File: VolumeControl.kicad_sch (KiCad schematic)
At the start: 8 parts, among them U6 NE5532, U7 NE5532

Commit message: Complete Volume Control
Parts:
- added C13, C19: 220u, symbol Device:C_Polarized
- added C14, C21: C, symbol Device:C
- added C15, C16, C22, C23: 100p, symbol Device:C
- added C17, C24: 470p, symbol Device:C
- added C18, C20: 100n, symbol Device:C
- added J1, J2: Conn_01x03, symbol Connector_Generic:Conn_01x03
- added R25, R31, R34, R35, R36, R37, R43: 1k, symbol Device:R
- added R26, R28, R38, R39: 5k6, symbol Device:R
- added R27, R29, R40, R41: 10, symbol Device:R
- added R30, R32, R42, R44: 3k3, symbol Device:R
- added R33: 47k, symbol Device:R
- added U8, U9: NE5532, symbol Amplifier_Operational:NE5532
- R21: value 10 -> 47k
- R22, R23, R24: value 10 -> 1k
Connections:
- net +15V: now also C18.1, C20.1, U8.8 (V+), U9.8 (V+)
- net GND: now also C18.2, C20.2, U8.4 (V-), U9.4 (V-)
- net INP_BUF_OUT_RIGHT: now also C19.1; no longer R21.2, R22.2, R23.2, R24.2
- net at U6.5 (+): now also R21.2, C14.2; no longer U6.3 (+)
- net at R22.1, U6.6 (-), U6.7: now also R25.1
- net at U7.5 (+): now also R31.1; no longer U7.3 (+)
- new net: C16.2, R28.1, R29.2, U7.1
- new net: C16.1, R25.2, R28.2, U7.2 (-)
- new net: C13.2, J1.1 (Pin_1)
- new net: J1.3 (Pin_3), R27.1, R29.1, R32.2
- new net: C22.1, R36.2, R38.2, U9.2 (-)
- new net: C22.2, R38.1, R40.2, U9.1
- new net: C17.1, R30.2, R32.1, U7.6 (-)
- new net: C15.1, R22.2, R26.2, U6.2 (-)
- new net: C15.2, R26.1, R27.2, U6.1
- new net: R23.1, U7.3 (+)
- new net: R34.1, U9.3 (+)
- new net: C23.2, R39.1, R41.2, U8.1
- new net: C23.1, R37.2, R39.2, U8.2 (-)
- new net: R35.1, U8.3 (+)
- new net: R36.1, R37.1, U9.6 (-), U9.7
- new net: C24.1, R42.1, R44.2, U8.6 (-)
- new net: J2.3 (Pin_3), R40.1, R41.1, R42.2
- new net: C21.2, R33.2, U9.5 (+)
- new net: R43.1, U8.5 (+)
- new net: R24.1, U6.3 (+)
- new net: C19.2, J2.1 (Pin_1)
- new net INP_BUF_OUT_LEFT: C13.1
- new net VAS_OUT_LEFT: C17.2, R30.1, U7.7
- new net VAS_OUT_RIGHT: C24.2, R44.1, U8.7
- new net VBIAS_LEFT: R21.1, R23.2, R24.2, R31.2
- new net VBIAS_RIGHT: R33.1, R34.2, R35.2, R43.2
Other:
- note added: "Baxandall Active Volume Control"
- moved on the sheet: C11, C12, R21, R22, U6A, U6B, U6C, U7B, U7C

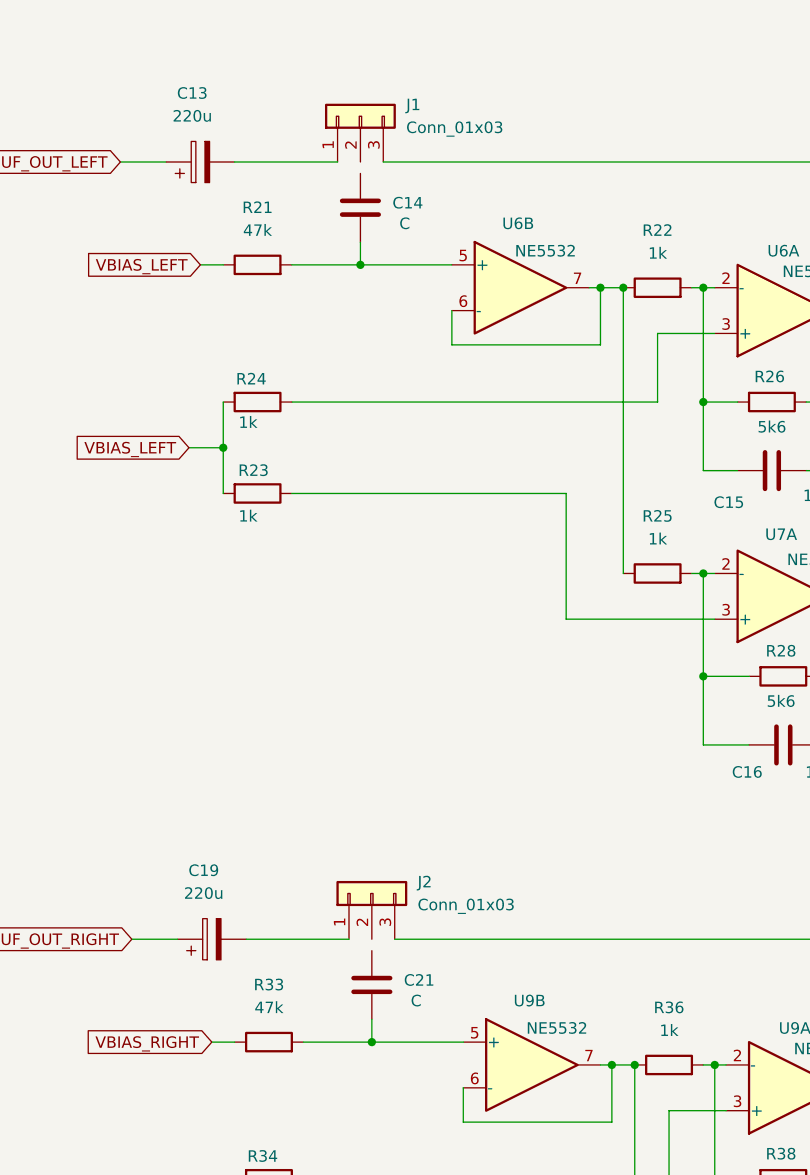
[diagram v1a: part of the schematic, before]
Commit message: Add missing C values
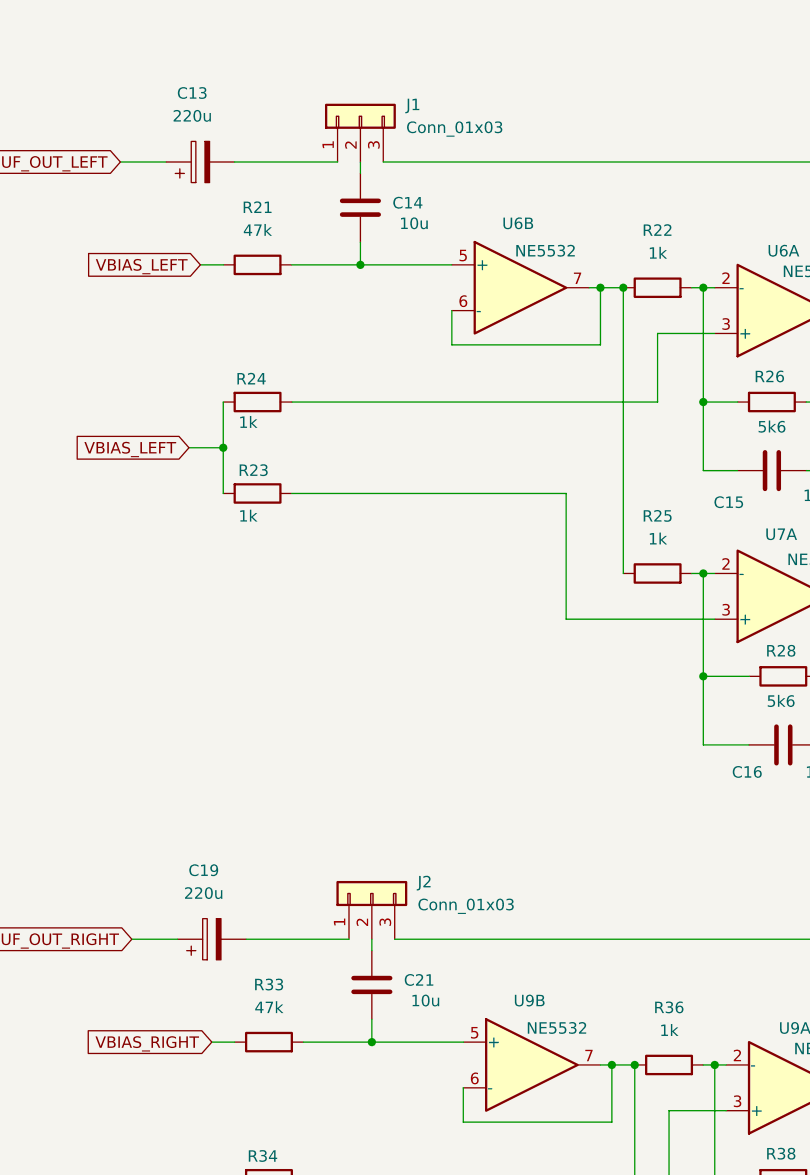
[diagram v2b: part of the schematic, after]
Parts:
- C14, C21: value C -> 10u
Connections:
- net at J1.2 (Pin_2): now also C14.1
- net at C21.1: now also J2.2 (Pin_2)
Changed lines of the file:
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@@
 	(wire
 		(pts
+			(xy 60.96 41.91) (xy 60.96 43.18)
+		)
+		(stroke
+			(width 0)
+			(type default)
+		)
+	)
+	(wire
+		(pts
 			(xy 127 58.42) (xy 127 41.91)
 		)
@@
 	(wire
 		(pts
+			(xy 62.23 128.27) (xy 62.23 129.54)
+		)
+		(stroke
+			(width 0)
+			(type default)
+		)
+	)
+	(wire
+		(pts
 			(xy 227.33 64.77) (xy 237.49 64.77)
 		)
@@
 			)
 		)
-		(property "Value" "C"
+		(property "Value" "10u"
 			(at 65.278 48.768 0)
 			(effects
@@
 			)
 		)
-		(property "Value" "C"
+		(property "Value" "10u"
 			(at 66.548 135.128 0)
 			(effects

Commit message: Add Footprints
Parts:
- C11, C12, C14, C15, C16, C17, C18, C20, C21, C22, C23, C24: footprint (none) -> Capacitor_SMD:C_0805_2012Metric
- C13, C19: footprint (none) -> Capacitor_SMD:CP_Elec_5x5.3
- J1, J2: footprint (none) -> TerminalBlock:TerminalBlock_bornier-3_P5.08mm
- R21, R22, R23, R24, R25, R26, R27, R28, R29, R30, R31, R32, R33, R34, R35, R36, R37, R38, R39, R40, R41, R42, R43, R44: footprint (none) -> Resistor_SMD:R_0805_2012Metric
- U6, U7, U8, U9: footprint (none) -> Package_SO:SOIC-8_3.9x4.9mm_P1.27mm
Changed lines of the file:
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@@
 			)
 		)
-		(property "Footprint" ""
+		(property "Footprint" "Resistor_SMD:R_0805_2012Metric"
 			(at 107.95 97.282 90)
 			(effects
@@
 			)
 		)
-		(property "Footprint" ""
+		(property "Footprint" "TerminalBlock:TerminalBlock_bornier-3_P5.08mm"
 			(at 60.96 36.83 0)
 			(effects
@@
 			)
 		)
-		(property "Footprint" ""
+		(property "Footprint" "Package_SO:SOIC-8_3.9x4.9mm_P1.27mm"
 			(at 215.9 53.34 0)
 			(effects
@@
 			)
 		)
-		(property "Footprint" ""
+		(property "Footprint" "Package_SO:SOIC-8_3.9x4.9mm_P1.27mm"
 			(at 240.03 53.34 0)
 			(effects
@@
 			)
 		)
-		(property "Footprint" ""
+		(property "Footprint" "Resistor_SMD:R_0805_2012Metric"
 			(at 141.478 33.02 90)
 			(effects
@@
 			)
 		)
-		(property "Footprint" ""
+		(property "Footprint" "Capacitor_SMD:C_0805_2012Metric"
 			(at 111.76 161.5948 0)
 			(effects
@@
 			)
 		)
-		(property "Footprint" ""
+		(property "Footprint" "Capacitor_SMD:C_0805_2012Metric"
 			(at 156.21 58.7248 0)
 			(effects
@@
 			)
 		)
-		(property "Footprint" ""
+		(property "Footprint" "Capacitor_SMD:C_0805_2012Metric"
 			(at 110.49 75.2348 0)
 			(effects
@@
 			)
 		)
-		(property "Footprint" ""
+		(property "Footprint" "Package_SO:SOIC-8_3.9x4.9mm_P1.27mm"
 			(at 107.95 96.52 0)
 			(effects
@@
 			)
 		)
-		(property "Footprint" ""
+		(property "Footprint" "Package_SO:SOIC-8_3.9x4.9mm_P1.27mm"
 			(at 109.22 151.13 0)
 			(effects
@@
 			)
 		)
-		(property "Footprint" ""
+		(property "Footprint" "Package_SO:SOIC-8_3.9x4.9mm_P1.27mm"
 			(at 109.22 182.88 0)
 			(effects
@@
 			)
 		)
-		(property "Footprint" ""
+		(property "Footprint" "Resistor_SMD:R_0805_2012Metric"
 			(at 95.25 144.018 90)
 			(effects
@@
 			)
 		)
-		(property "Footprint" ""
+		(property "Footprint" "Package_SO:SOIC-8_3.9x4.9mm_P1.27mm"
 			(at 78.74 55.88 0)
 			(effects
@@
 			)
 		)
-		(property "Footprint" ""
+		(property "Footprint" "Resistor_SMD:R_0805_2012Metric"
 			(at 152.4 51.562 90)
 			(effects
@@
 			)
 		)
-		(property "Footprint" ""
+		(property "Footprint" "Resistor_SMD:R_0805_2012Metric"
 			(at 107.95 153.162 90)
 			(effects
@@
 			)
 		)
-		(property "Footprint" ""
+		(property "Footprint" "Capacitor_SMD:C_0805_2012Metric"
 			(at 61.9252 50.8 0)
 			(effects
@@
 			)
 		)
-		(property "Footprint" ""
+		(property "Footprint" "Capacitor_SMD:C_0805_2012Metric"
 			(at 205.4352 138.43 0)
 			(effects
@@
 			)
 		)
-		(property "Footprint" ""
+		(property "Footprint" "Resistor_SMD:R_0805_2012Metric"
 			(at 134.62 126.492 90)
 			(effects
@@
 			)
 		)
-		(property "Footprint" ""
+		(property "Footprint" "Resistor_SMD:R_0805_2012Metric"
 			(at 50.8 163.322 90)
 			(effects
@@
 			)
 		)
-		(property "Footprint" ""
+		(property "Footprint" "Resistor_SMD:R_0805_2012Metric"
 			(at 121.92 56.642 90)
 			(effects
@@
 			)
 		)
-		(property "Footprint" ""
+		(property "Footprint" "Capacitor_SMD:C_0805_2012Metric"
 			(at 111.76 105.7148 0)
 			(effects
@@
 			)
 		)
-		(property "Footprint" ""
+		(property "Footprint" "Resistor_SMD:R_0805_2012Metric"
 			(at 50.8 141.478 90)
 			(effects
@@
 			)
 		)
-		(property "Footprint" ""
+		(property "Footprint" "Resistor_SMD:R_0805_2012Metric"
 			(at 95.25 175.768 90)
 			(effects
@@
 			)
 		)
-		(property "Footprint" ""
+		(property "Footprint" "Package_SO:SOIC-8_3.9x4.9mm_P1.27mm"
 			(at 80.01 142.24 0)
 			(effects
@@
 			)
 		)
-		(property "Footprint" ""
+		(property "Footprint" "Capacitor_SMD:C_0805_2012Metric"
 			(at 157.48 145.0848 0)
 			(effects
@@
 			)
 		)
-		(property "Footprint" ""
+		(property "Footprint" "Resistor_SMD:R_0805_2012Metric"
 			(at 142.748 119.38 90)
 			(effects
@@
 			)
 		)
-		(property "Footprint" ""
+		(property "Footprint" "Package_SO:SOIC-8_3.9x4.9mm_P1.27mm"
 			(at 107.95 64.77 0)
 			(effects
@@
 			)
 		)
-		(property "Footprint" ""
+		(property "Footprint" "Resistor_SMD:R_0805_2012Metric"
 			(at 50.8 153.162 90)
 			(effects
@@
 			)
 		)
-		(property "Footprint" ""
+		(property "Footprint" "Package_SO:SOIC-8_3.9x4.9mm_P1.27mm"
 			(at 241.3 133.35 0)
 			(effects
@@
 			)
 		)
-		(property "Footprint" ""
+		(property "Footprint" "Resistor_SMD:R_0805_2012Metric"
 			(at 49.53 55.118 90)
 			(effects
@@
 			)
 		)
-		(property "Footprint" ""
+		(property "Footprint" "Package_SO:SOIC-8_3.9x4.9mm_P1.27mm"
 			(at 217.17 133.35 0)
 			(effects
@@
 			)
 		)
-		(property "Footprint" ""
+		(property "Footprint" "Resistor_SMD:R_0805_2012Metric"
 			(at 121.92 88.392 90)
 			(effects
@@
 			)
 		)
-		(property "Footprint" ""
+		(property "Footprint" "Resistor_SMD:R_0805_2012Metric"
 			(at 49.53 76.962 90)
 			(effects
@@
 			)
 		)
-		(property "Footprint" ""
+		(property "Footprint" "Resistor_SMD:R_0805_2012Metric"
 			(at 93.98 89.408 90)
 			(effects
@@
 			)
 		)
-		(property "Footprint" ""
+		(property "Footprint" "Resistor_SMD:R_0805_2012Metric"
 			(at 133.35 40.132 90)
 			(effects
@@
 			)
 		)
-		(property "Footprint" ""
+		(property "Footprint" "Resistor_SMD:R_0805_2012Metric"
 			(at 49.53 66.802 90)
 			(effects
@@
 			)
 		)
-		(property "Footprint" ""
+		(property "Footprint" "Capacitor_SMD:C_0805_2012Metric"
 			(at 63.1952 137.16 0)
 			(effects
@@
 			)
 		)
-		(property "Footprint" ""
+		(property "Footprint" "Resistor_SMD:R_0805_2012Metric"
 			(at 93.98 57.658 90)
 			(effects
@@
 			)
 		)
-		(property "Footprint" ""
+		(property "Footprint" "TerminalBlock:TerminalBlock_bornier-3_P5.08mm"
 			(at 62.23 123.19 0)
 			(effects
@@
 			)
 		)
-		(property "Footprint" ""
+		(property "Footprint" "Capacitor_SMD:CP_Elec_5x5.3"
 			(at 46.99 40.9448 0)
 			(effects
@@
 			)
 		)
-		(property "Footprint" ""
+		(property "Footprint" "Resistor_SMD:R_0805_2012Metric"
 			(at 153.67 137.922 90)
 			(effects
@@
 			)
 		)
-		(property "Footprint" ""
+		(property "Footprint" "Package_SO:SOIC-8_3.9x4.9mm_P1.27mm"
 			(at 153.67 39.37 0)
 			(effects
@@
 			)
 		)
-		(property "Footprint" ""
+		(property "Footprint" "Package_SO:SOIC-8_3.9x4.9mm_P1.27mm"
 			(at 154.94 125.73 0)
 			(effects
@@
 			)
 		)
-		(property "Footprint" ""
+		(property "Footprint" "Capacitor_SMD:C_0805_2012Metric"
 			(at 204.1652 58.42 0)
 			(effects
@@
 			)
 		)
-		(property "Footprint" ""
+		(property "Footprint" "Resistor_SMD:R_0805_2012Metric"
 			(at 123.19 143.002 90)
 			(effects
@@
 			)
 		)
-		(property "Footprint" ""
+		(property "Footprint" "Resistor_SMD:R_0805_2012Metric"
 			(at 106.68 66.802 90)
 			(effects
@@
 			)
 		)
-		(property "Footprint" ""
+		(property "Footprint" "Capacitor_SMD:C_0805_2012Metric"
 			(at 113.03 192.0748 0)
 			(effects
@@
 			)
 		)
-		(property "Footprint" ""
+		(property "Footprint" "Capacitor_SMD:C_0805_2012Metric"
 			(at 228.2952 58.42 0)
 			(effects
@@
 			)
 		)
-		(property "Footprint" ""
+		(property "Footprint" "Capacitor_SMD:C_0805_2012Metric"
 			(at 229.5652 138.43 0)
 			(effects
@@
 			)
 		)
-		(property "Footprint" ""
+		(property "Footprint" "Resistor_SMD:R_0805_2012Metric"
 			(at 123.19 174.752 90)
 			(effects
@@
 			)
 		)
-		(property "Footprint" ""
+		(property "Footprint" "Resistor_SMD:R_0805_2012Metric"
 			(at 109.22 183.642 90)
 			(effects
@@
 			)
 		)
-		(property "Footprint" ""
+		(property "Footprint" "Capacitor_SMD:CP_Elec_5x5.3"
 			(at 48.26 127.3048 0)
 			(effects
